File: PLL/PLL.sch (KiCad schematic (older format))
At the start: 78 parts, among them J1 Clock, J10 Mix, J2 EuroPower, J3 M8, J4 M4, J5 M2, J6 M1, J7 D2, J8 D4, J9 D8, SW1 Freq range, U1 TL082, U2 CD4046, U3 CD4040

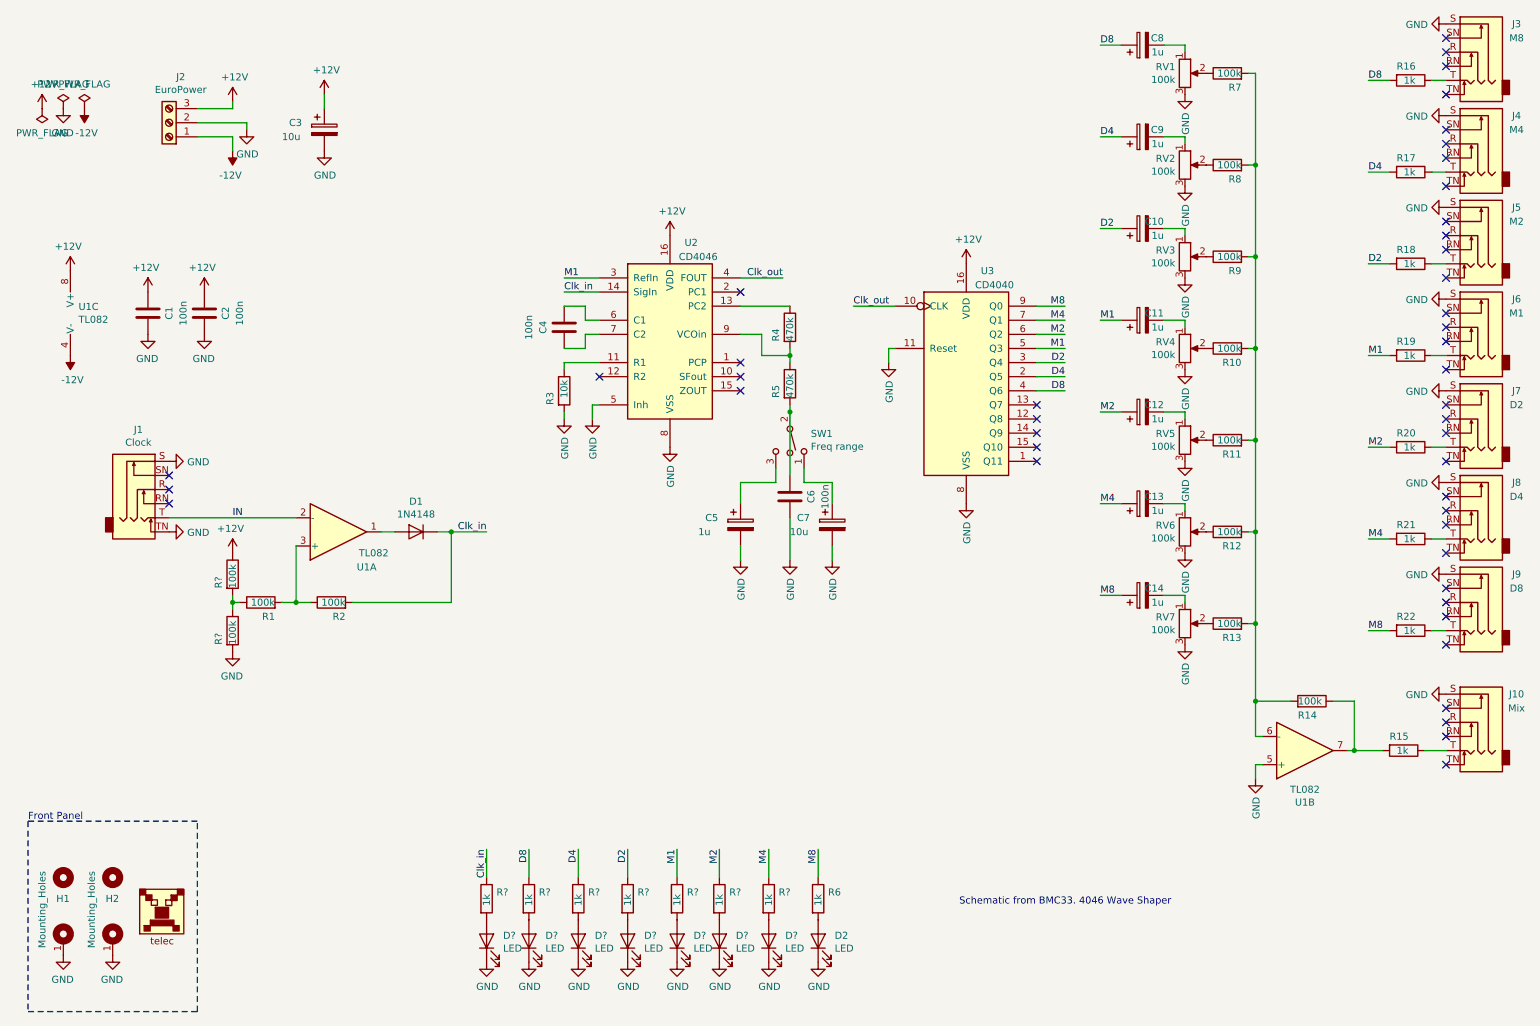
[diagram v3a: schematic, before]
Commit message: File restructuration
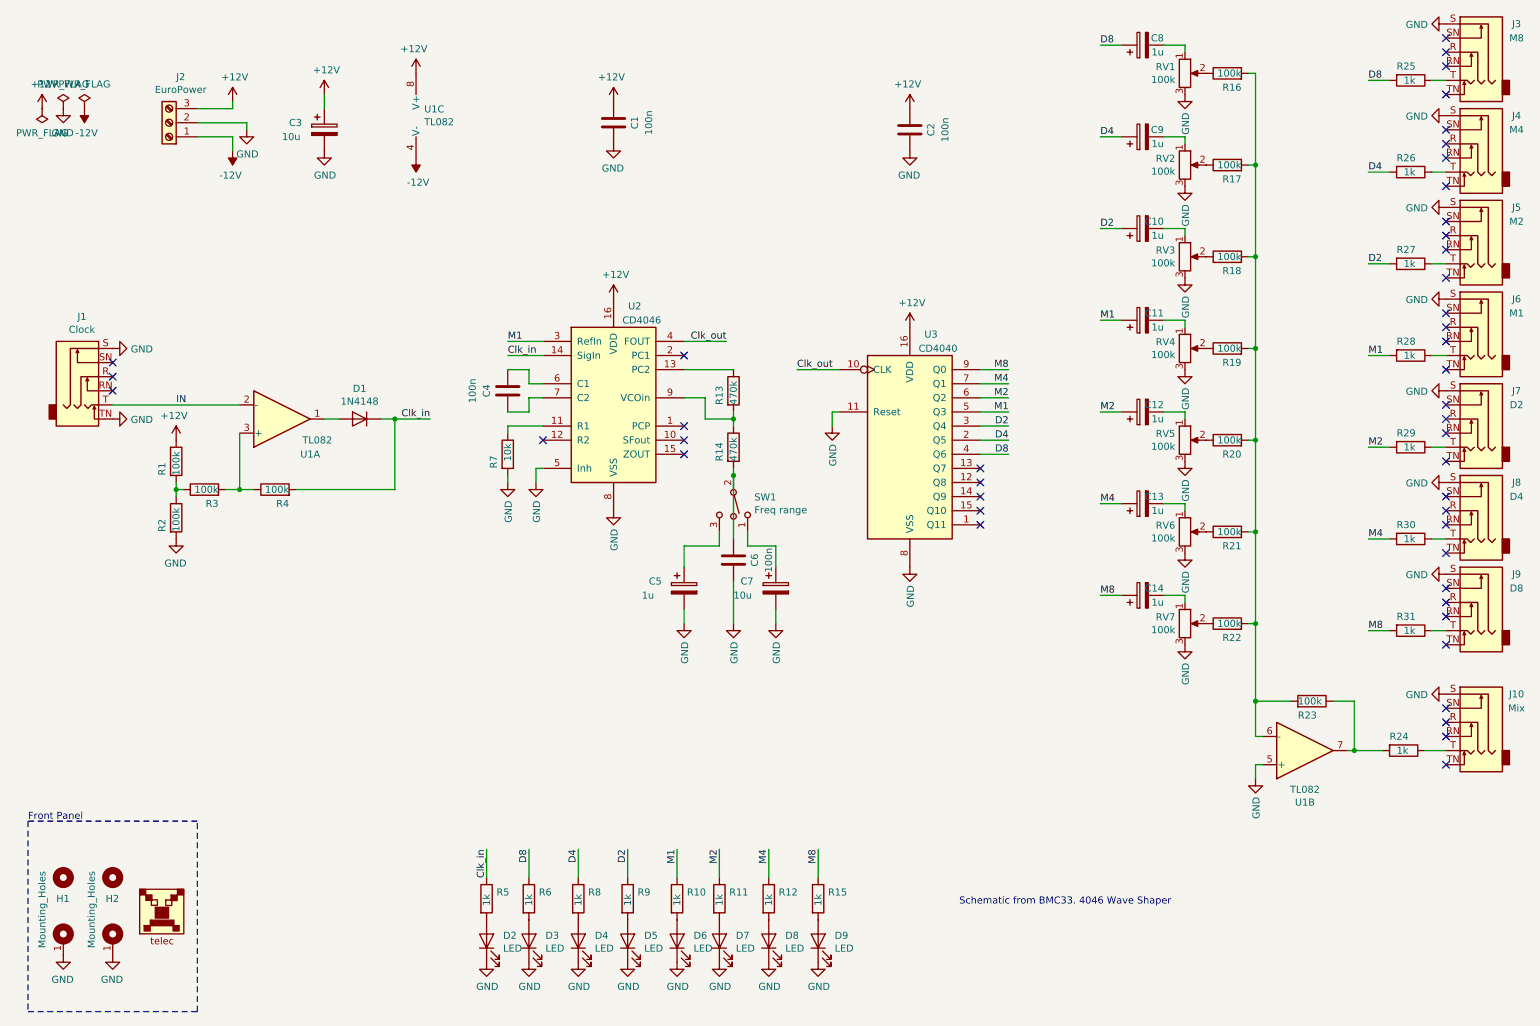
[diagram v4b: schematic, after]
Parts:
- gave numbers to parts that had none: 16
- renumbered D2 to D9, R4 to R13, R5 to R14, R6 to R15, R7 to R16, R8 to R17, R9 to R18, R10 to R19, R11 to R20, R12 to R21, R13 to R22, R14 to R23, R15 to R24, R16 to R25, R17 to R26, R18 to R27, R19 to R28, R20 to R29, R1 to R3, R21 to R30, R22 to R31, R2 to R4, R3 to R7
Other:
- moved on the sheet: C1, C2, C4, C5, C6, C7, D1, J1, R1, R13, R14, R2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

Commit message: PLL done !
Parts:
- J3: value M8 -> D8
- J4: value M4 -> D4
- J5: value M2 -> D2
- J7: value D2 -> M2
- J8: value D4 -> M4
- J9: value D8 -> M8
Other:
- note added: "Hysteresis input"
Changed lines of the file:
@@
 P 10800 800
 F 0 "J3" H 10500 1000 50  0000 C CNN
-F 1 "M8" H 10500 900 50  0000 C CNN
+F 1 "D8" H 10500 900 50  0000 C CNN
 F 2 "telec:JackHole" H 10800 800 50  0001 C CNN
 F 3 "~" H 10800 800 50  0001 C CNN
@@
 P 10800 1450
 F 0 "J4" H 10500 1650 50  0000 C CNN
-F 1 "M4" H 10500 1550 50  0000 C CNN
+F 1 "D4" H 10500 1550 50  0000 C CNN
 F 2 "telec:JackHole" H 10800 1450 50  0001 C CNN
 F 3 "~" H 10800 1450 50  0001 C CNN
@@
 P 10800 2100
 F 0 "J5" H 10500 2300 50  0000 C CNN
-F 1 "M2" H 10500 2200 50  0000 C CNN
+F 1 "D2" H 10500 2200 50  0000 C CNN
 F 2 "telec:JackHole" H 10800 2100 50  0001 C CNN
 F 3 "~" H 10800 2100 50  0001 C CNN
@@
 P 10800 3400
 F 0 "J7" H 10500 3600 50  0000 C CNN
-F 1 "D2" H 10500 3500 50  0000 C CNN
+F 1 "M2" H 10500 3500 50  0000 C CNN
 F 2 "telec:JackHole" H 10800 3400 50  0001 C CNN
 F 3 "~" H 10800 3400 50  0001 C CNN
@@
 P 10800 4050
 F 0 "J8" H 10500 4250 50  0000 C CNN
-F 1 "D4" H 10500 4150 50  0000 C CNN
+F 1 "M4" H 10500 4150 50  0000 C CNN
 F 2 "telec:JackHole" H 10800 4050 50  0001 C CNN
 F 3 "~" H 10800 4050 50  0001 C CNN
@@
 P 10800 4700
 F 0 "J9" H 10500 4900 50  0000 C CNN
-F 1 "D8" H 10500 4800 50  0000 C CNN
+F 1 "M8" H 10500 4800 50  0000 C CNN
 F 2 "telec:JackHole" H 10800 4700 50  0001 C CNN
 F 3 "~" H 10800 4700 50  0001 C CNN
@@
 Wire Wire Line
 	8600 750  8750 750
-$Comp
-L Device:CP C9
-U 1 1 62AE5BC7
-P 8450 1400
-F 0 "C9" V 8500 1250 50  0000 L CNN
-F 1 "1u" V 8400 1250 50  0000 L CNN
-F 2 "Capacitor_THT:CP_Radial_D4.0mm_P1.50mm" H 8488 1250 50  0001 C CNN
-F 3 "~" H 8450 1400 50  0001 C CNN
-	1    8450 1400
-	0    -1   -1   0
-$EndComp
 Wire Wire Line
 	8600 1400 8750 1400
@@
 U 1 1 62AE6033
 P 8450 2050
-F 0 "C10" V 8500 1900 50  0000 L CNN
+F 0 "C10" V 8500 1850 50  0000 L CNN
 F 1 "1u" V 8400 1900 50  0000 L CNN
 F 2 "Capacitor_THT:CP_Radial_D4.0mm_P1.50mm" H 8488 1900 50  0001 C CNN
@@
 U 1 1 62AE6B6D
 P 8450 2700
-F 0 "C11" V 8500 2550 50  0000 L CNN
+F 0 "C11" V 8500 2500 50  0000 L CNN
 F 1 "1u" V 8400 2550 50  0000 L CNN
 F 2 "Capacitor_THT:CP_Radial_D4.0mm_P1.50mm" H 8488 2550 50  0001 C CNN
@@
 U 1 1 62AE755D
 P 8450 3350
-F 0 "C12" V 8500 3200 50  0000 L CNN
+F 0 "C12" V 8500 3150 50  0000 L CNN
 F 1 "1u" V 8400 3200 50  0000 L CNN
 F 2 "Capacitor_THT:CP_Radial_D4.0mm_P1.50mm" H 8488 3200 50  0001 C CNN
@@
 U 1 1 62AE82B5
 P 8450 4000
-F 0 "C13" V 8500 3850 50  0000 L CNN
+F 0 "C13" V 8500 3800 50  0000 L CNN
 F 1 "1u" V 8400 3850 50  0000 L CNN
 F 2 "Capacitor_THT:CP_Radial_D4.0mm_P1.50mm" H 8488 3850 50  0001 C CNN
@@
 U 1 1 62AE8B79
 P 8450 4650
-F 0 "C14" V 8500 4500 50  0000 L CNN
+F 0 "C14" V 8500 4450 50  0000 L CNN
 F 1 "1u" V 8400 4500 50  0000 L CNN
 F 2 "Capacitor_THT:CP_Radial_D4.0mm_P1.50mm" H 8488 4500 50  0001 C CNN
@@
 Text Label 4100 6450 3    50   ~ 0
 D8
+$Comp
+L Device:CP C9
+U 1 1 62AE5BC7
+P 8450 1400
+F 0 "C9" V 8500 1250 50  0000 L CNN
+F 1 "1u" V 8400 1250 50  0000 L CNN
+F 2 "Capacitor_THT:CP_Radial_D4.0mm_P1.50mm" H 8488 1250 50  0001 C CNN
+F 3 "~" H 8450 1400 50  0001 C CNN
+	1    8450 1400
+	0    -1   -1   0
+$EndComp
+Text Notes 2100 2950 0    50   ~ 0
+Hysteresis input
 $EndSCHEMATC

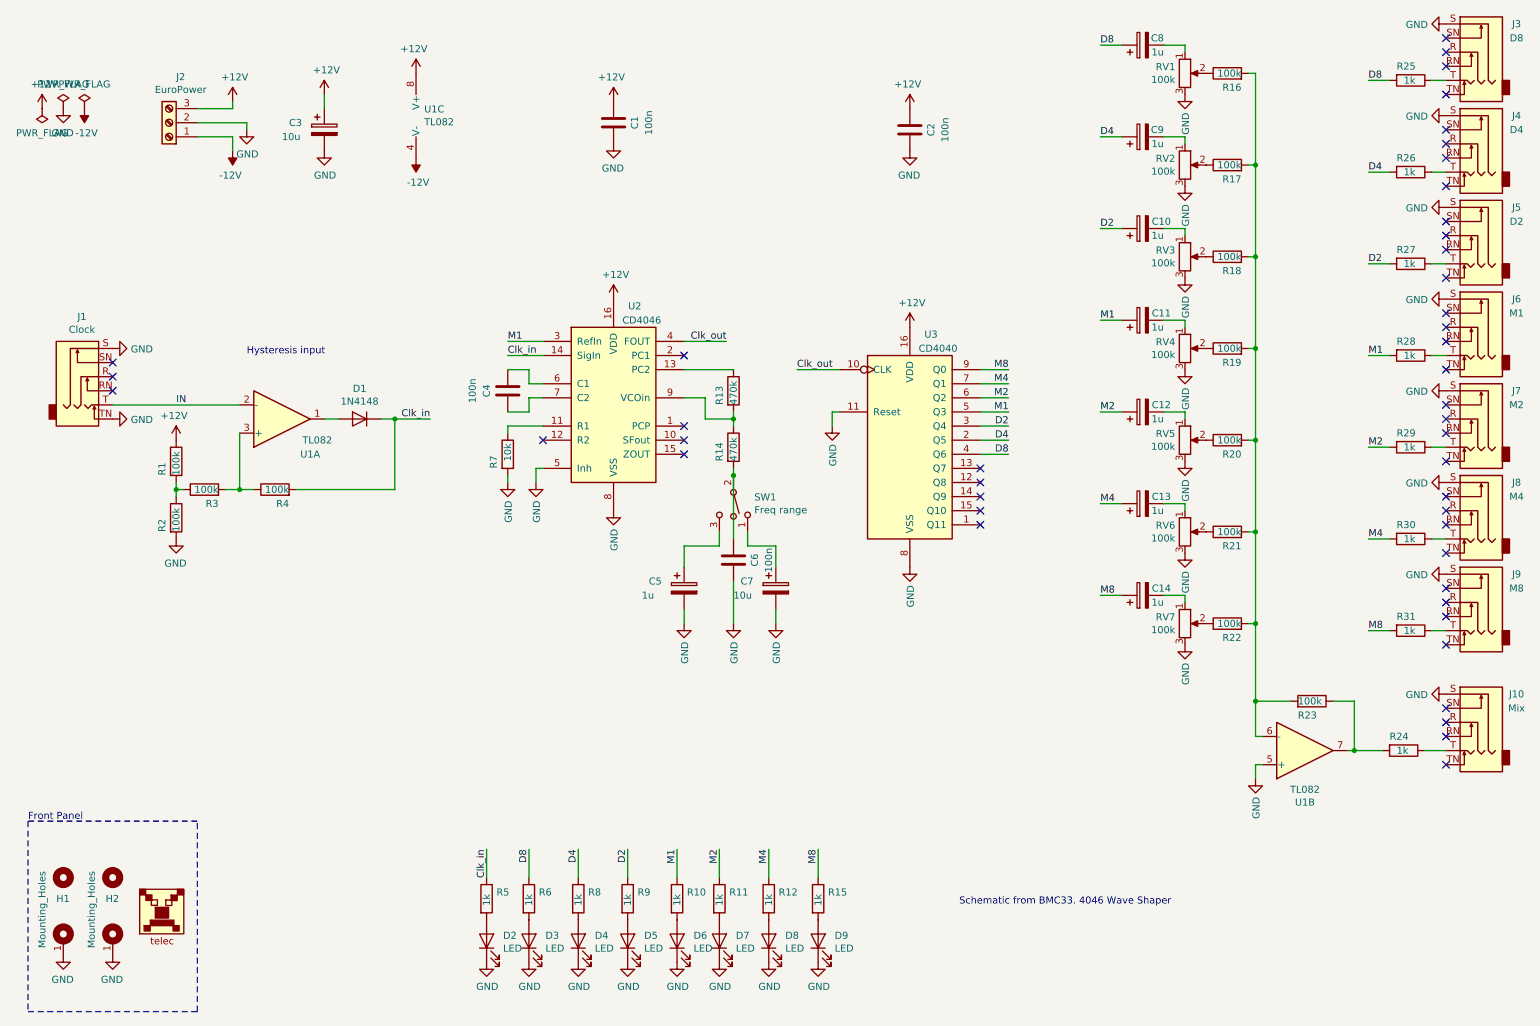
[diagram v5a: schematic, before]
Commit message: Analog modules finished
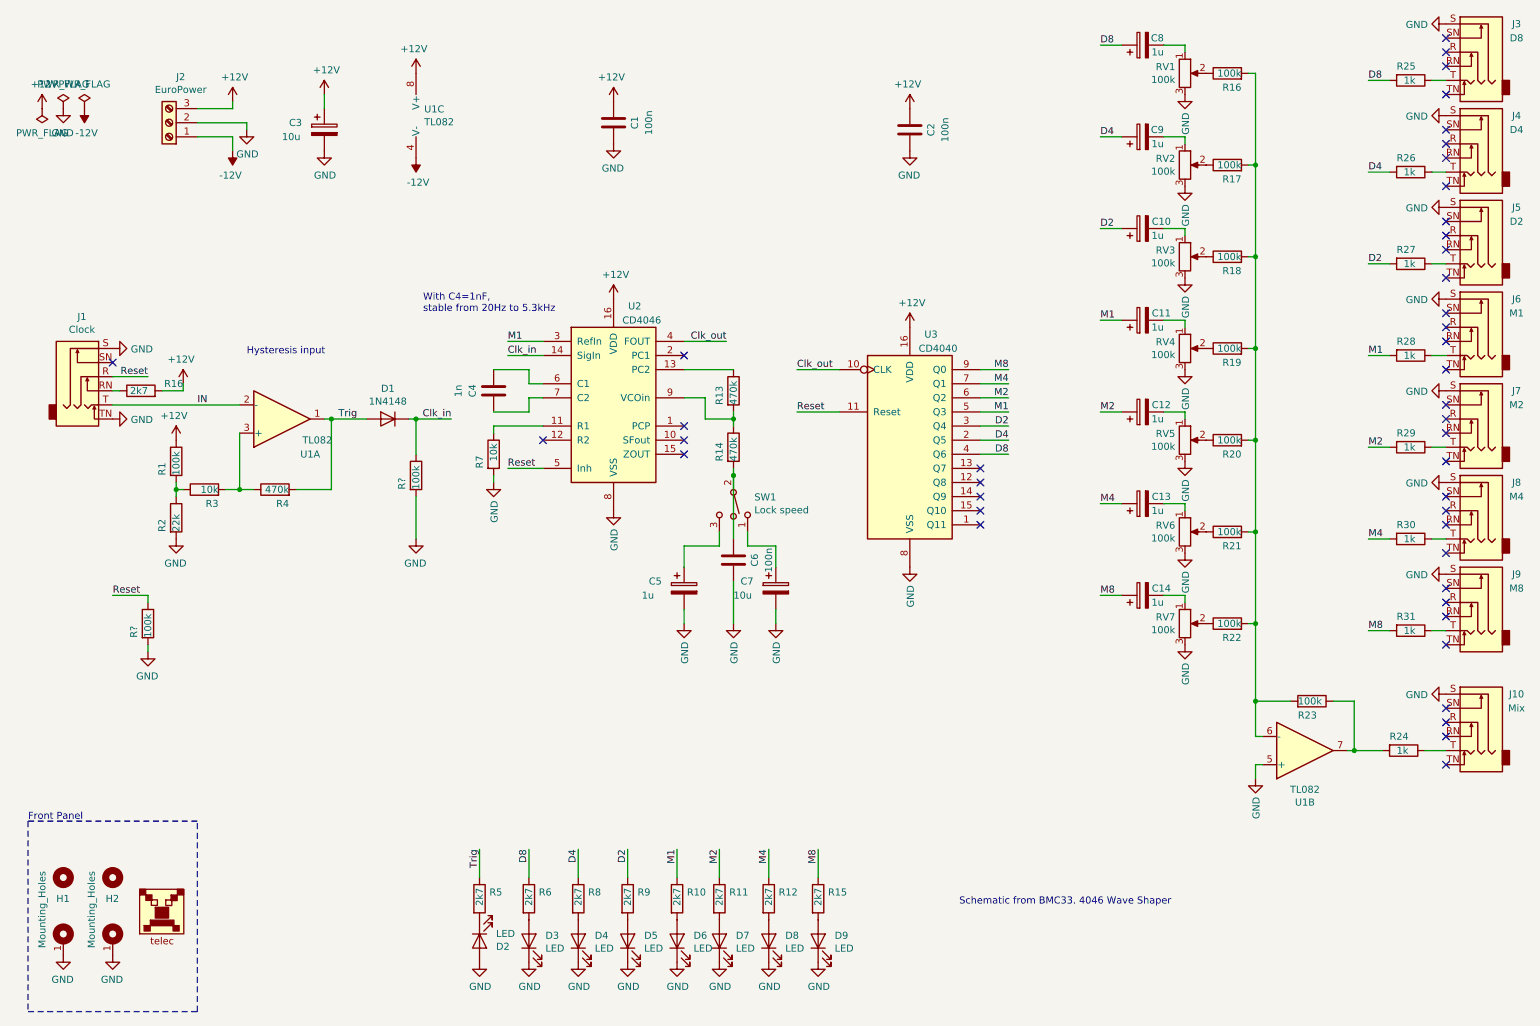
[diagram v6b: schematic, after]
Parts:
- added R16: 2k7, Resistor_SMD:R_1206_3216Metric_Pad1.42x1.75mm_HandSolder, symbol Device:R
- added R? (x2): 100k, Resistor_SMD:R_1206_3216Metric_Pad1.42x1.75mm_HandSolder, symbol Device:R
- C4: value 100n -> 1n
- R10, R11, R12, R15, R5, R6, R8, R9: value 1k -> 2k7
- R2: value 100k -> 22k
- R3: value 100k -> 10k
- R4: value 100k -> 470k
- SW1: value Freq range -> Lock speed
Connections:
- net +12V: now also R16.2
- net Clk_in: now also R?.1; no longer R4.2, R5.1
- net GND: now also D2.2 (A), R?.2, R?.2; no longer D2.1 (K), U2.5 (Inh), U3.11 (Reset)
- net Reset: now reaches J1.R
- net Reset: now also U2.5 (Inh), U3.11 (Reset), R?.1
- net at J1.RN: now also R16.1
- net Trig: now reaches D1.2 (A), U1.1
- net Trig: now also R4.2, R5.1
- net at R5.2: now also D2.1 (K); no longer D2.2 (A)
- no-connect marks 45 -> 43
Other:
- note added: "With C4=1nF,\nstable from 20Hz to 5.3kHz"
- moved on the sheet: C4, D1, D2, R5, R7

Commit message: Started PLL layout
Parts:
- J1, J10, J3, J4, J5, J6, J7, J8, J9: footprint telec:JackHole -> telec:Jack_Hole_Square; symbol Connector:AudioJack3_Switch -> Connector:AudioJack3_SwitchTR
- RV1, RV2, RV3, RV4, RV5, RV6, RV7: footprint Potentiometer_THT:Potentiometer_Piher_T-16L_Single_Vertical_Hole -> telec:Potentiometer_Single_Vertical_Hole
- gave numbers to parts that had none: 2
- renumbered C3 to C1, C4 to C2, C1 to C3, C5 to C4, C6 to C5, C7 to C6, C2 to C7, R6 to R10, R8 to R11, R9 to R12, R10 to R13, R11 to R14, R13 to R15, R14 to R16, R12 to R17, R15 to R18, R16 to R19, R16 to R2, R17 to R20, R18 to R21, R19 to R22, R20 to R23, R21 to R24, R22 to R25, R23 to R26, R24 to R27, R25 to R28, R26 to R29, R1 to R3, R27 to R30, R28 to R31, R29 to R32, R30 to R33, R31 to R34, R2 to R4, R3 to R5, R4 to R6, R5 to R8, R7 to R9
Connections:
- no-connect marks 43 -> 34
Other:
- moved on the sheet: R1

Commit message: PLL done
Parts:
- R1, R2: footprint Resistor_SMD:R_1206_3216Metric_Pad1.42x1.75mm_HandSolder -> Resistor_THT:R_Axial_DIN0204_L3.6mm_D1.6mm_P7.62mm_Horizontal
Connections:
- net +12V: now also R2.1; no longer R2.2
- net at J1.RN: now also R2.2; no longer R2.1
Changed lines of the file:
@@
-$EndComp
-$Comp
-L Device:R R2
-U 1 1 5F835D57
-P 1350 3200
-AR Path="/5F835D57" Ref="R2"  Part="1"
-AR Path="/5F42563C/5F835D57" Ref="R?"  Part="1"
-F 0 "R2" V 1400 2900 50  0000 L CNN
-F 1 "2k7" V 1350 3150 50  0000 L CNN
-F 2 "Resistor_SMD:R_1206_3216Metric_Pad1.42x1.75mm_HandSolder" V 1280 3200 50  0001 C CNN
-F 3 "~" H 1350 3200 50  0001 C CNN
-	1    1350 3200
-	0    -1   -1   0
 $EndComp
 $Comp
@@
 Wire Wire Line
 	1300 3850 1300 3900
-$Comp
-L Device:R R1
-U 1 1 5F89F815
-P 1300 4050
-AR Path="/5F89F815" Ref="R1"  Part="1"
-AR Path="/5F42563C/5F89F815" Ref="R?"  Part="1"
-AR Path="/5F425067/5F89F815" Ref="R?"  Part="1"
-F 0 "R1" V 1200 3950 50  0000 L CNN
-F 1 "100k" V 1300 3950 50  0000 L CNN
-F 2 "Resistor_SMD:R_1206_3216Metric_Pad1.42x1.75mm_HandSolder" V 1230 4050 50  0001 C CNN
-F 3 "~" H 1300 4050 50  0001 C CNN
-	1    1300 4050
-	1    0    0    -1
-$EndComp
 Wire Wire Line
 	1300 4250 1300 4200
@@
 	1    0    0    -1
 $EndComp
+$Comp
+L Device:R R1
+U 1 1 5F9EC571
+P 1300 4050
+AR Path="/5F9EC571" Ref="R1"  Part="1"
+AR Path="/5F42563C/5F9EC571" Ref="R?"  Part="1"
+AR Path="/5F425067/5F9EC571" Ref="R?"  Part="1"
+F 0 "R1" V 1200 3950 50  0000 L CNN
+F 1 "100k" V 1300 3950 50  0000 L CNN
+F 2 "Resistor_THT:R_Axial_DIN0204_L3.6mm_D1.6mm_P7.62mm_Horizontal" V 1230 4050 50  0001 C CNN
+F 3 "~" H 1300 4050 50  0001 C CNN
+	1    1300 4050
+	1    0    0    -1
+$EndComp
+$Comp
+L Device:R R2
+U 1 1 5F9EDF49
+P 1350 3200
+AR Path="/5F9EDF49" Ref="R2"  Part="1"
+AR Path="/5F42563C/5F9EDF49" Ref="R?"  Part="1"
+AR Path="/5F425067/5F9EDF49" Ref="R?"  Part="1"
+F 0 "R2" V 1300 3350 50  0000 L CNN
+F 1 "2k7" V 1350 3150 50  0000 L CNN
+F 2 "Resistor_THT:R_Axial_DIN0204_L3.6mm_D1.6mm_P7.62mm_Horizontal" V 1280 3200 50  0001 C CNN
+F 3 "~" H 1350 3200 50  0001 C CNN
+	1    1350 3200
+	0    1    1    0
+$EndComp
 $EndSCHEMATC
